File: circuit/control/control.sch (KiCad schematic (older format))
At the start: 24 parts

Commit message: [update] update the circuit diagram
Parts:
- removed 270Ω, 270Ω? (x2): R_US, symbol Device:R_US
- added 270Ω (x4), 270Ω? (x4): R_US, symbol Device:R_US
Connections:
- net GNDPWR: now also 270Ω.2, 270Ω.2, 270Ω.2
- net at RED.1 (K): now also 270Ω.1
- net at GREEN.1 (K): now also 270Ω.1
- net at YELLOW.1 (K): now also 270Ω.1
- net at primary.1 (QB): now also 270Ω?.2; no longer Q?.3 (B)
- net at primary.15 (QA): now also 270Ω?.2; no longer Q?.3 (B)
- net at primary.2 (QC): now also 270Ω?.2; no longer Q?.3 (B)
- net at primary.3 (QD): now also 270Ω?.2; no longer Q?.3 (B)
- net at primary.4 (QE): now also 270Ω.2; no longer Q?.3 (B)
- new net: 270Ω?.1, Q?.3 (B) (x4)
- new net: 270Ω.1, Q?.3 (B)
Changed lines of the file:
@@
 Wire Wire Line
 	8250 3850 8250 5100
-$Comp
-L Device:R_US 270Ω
-U 1 1 6139C615
-P 9750 4650
-F 0 "270Ω" H 9818 4696 50  0000 L CNN
-F 1 "R_US" H 9818 4605 50  0000 L CNN
-F 2 "" V 9790 4640 50  0001 C CNN
-F 3 "~" H 9750 4650 50  0001 C CNN
-	1    9750 4650
-	1    0    0    -1
-$EndComp
 Wire Wire Line
 	9750 4350 9750 4500
-$Comp
-L Device:R_US 270Ω?
-U 1 1 613AA82A
-P 9300 4650
-F 0 "270Ω?" H 9368 4696 50  0000 L CNN
-F 1 "R_US" H 9368 4605 50  0000 L CNN
-F 2 "" V 9340 4640 50  0001 C CNN
-F 3 "~" H 9300 4650 50  0001 C CNN
-	1    9300 4650
-	1    0    0    -1
-$EndComp
 Wire Wire Line
 	9300 4350 9300 4500
@@
 Wire Wire Line
 	9300 4800 9300 5250
-$Comp
-L Device:R_US 270Ω?
-U 1 1 613AB612
-P 8850 4650
-F 0 "270Ω?" H 8918 4696 50  0000 L CNN
-F 1 "R_US" H 8918 4605 50  0000 L CNN
-F 2 "" V 8890 4640 50  0001 C CNN
-F 3 "~" H 8850 4650 50  0001 C CNN
-	1    8850 4650
-	1    0    0    -1
-$EndComp
 Wire Wire Line
 	8850 4350 8850 4500
@@
 	9650 1950 9650 2600
 Wire Wire Line
-	6750 2150 6750 3850
-Wire Wire Line
-	6850 3850 6850 2950
-Wire Wire Line
 	6850 2950 9350 2950
 Wire Wire Line
 	9350 2950 9350 1750
 Wire Wire Line
-	6950 3850 6950 3100
-Wire Wire Line
 	6950 3100 8700 3100
 Wire Wire Line
 	8700 3100 8700 1850
 Wire Wire Line
-	7050 3850 7050 3250
-Wire Wire Line
 	7050 3250 7950 3250
 Wire Wire Line
@@
 Wire Wire Line
 	7250 3400 7150 3400
-Wire Wire Line
-	7150 3400 7150 3850
 Wire Wire Line
 	7250 2050 7250 3400
@@
 Wire Wire Line
 	2650 2550 2650 2900
+$Comp
+L Device:R_US 270Ω?
+U 1 1 61287539
+P 6850 3600
+F 0 "270Ω?" H 6918 3646 50  0001 L CNN
+F 1 "R_US" H 6918 3555 50  0001 L CNN
+F 2 "" V 6890 3590 50  0001 C CNN
+F 3 "~" H 6850 3600 50  0001 C CNN
+	1    6850 3600
+	1    0    0    -1
+$EndComp
+$Comp
+L Device:R_US 270Ω?
+U 1 1 6128753F
+P 6950 3600
+F 0 "270Ω?" H 7018 3646 50  0001 L CNN
+F 1 "R_US" H 7018 3555 50  0001 L CNN
+F 2 "" V 6990 3590 50  0001 C CNN
+F 3 "~" H 6950 3600 50  0001 C CNN
+	1    6950 3600
+	1    0    0    -1
+$EndComp
+$Comp
+L Device:R_US 270Ω?
+U 1 1 61287545
+P 7050 3600
+F 0 "270Ω?" H 7118 3646 50  0001 L CNN
+F 1 "R_US" H 7118 3555 50  0001 L CNN
+F 2 "" V 7090 3590 50  0001 C CNN
+F 3 "~" H 7050 3600 50  0001 C CNN
+	1    7050 3600
+	1    0    0    -1
+$EndComp
+Wire Wire Line
+	6750 3750 6750 3850
+Wire Wire Line
+	6850 3750 6850 3850
+Wire Wire Line
+	6950 3750 6950 3850
+Wire Wire Line
+	7050 3850 7050 3750
+Wire Wire Line
+	7150 3750 7150 3850
+Wire Wire Line
+	7150 3450 7150 3400
+Wire Wire Line
+	6850 2950 6850 3450
+Wire Wire Line
+	6950 3450 6950 3100
+Wire Wire Line
+	7050 3250 7050 3450
+$Comp
+L Device:R_US 270Ω
+U 1 1 6128754B
+P 7150 3600
+F 0 "270Ω" H 7218 3646 50  0000 L CNN
+F 1 "R_US" H 7218 3555 50  0000 L CNN
+F 2 "" V 7190 3590 50  0001 C CNN
+F 3 "~" H 7150 3600 50  0001 C CNN
+	1    7150 3600
+	1    0    0    -1
+$EndComp
+$Comp
+L Device:R_US 270Ω?
+U 1 1 61287533
+P 6750 3600
+F 0 "270Ω?" H 6818 3646 50  0001 L CNN
+F 1 "R_US" H 6818 3555 50  0001 L CNN
+F 2 "" V 6790 3590 50  0001 C CNN
+F 3 "~" H 6750 3600 50  0001 C CNN
+	1    6750 3600
+	1    0    0    -1
+$EndComp
+Wire Wire Line
+	6750 3450 6750 2150
+$Comp
+L Device:R_US 270Ω
+U 1 1 612C32C9
+P 8850 4650
+F 0 "270Ω" H 8918 4696 50  0000 L CNN
+F 1 "R_US" H 8918 4605 50  0000 L CNN
+F 2 "" V 8890 4640 50  0001 C CNN
+F 3 "~" H 8850 4650 50  0001 C CNN
+	1    8850 4650
+	1    0    0    -1
+$EndComp
+$Comp
+L Device:R_US 270Ω
+U 1 1 612C81D5
+P 9300 4650
+F 0 "270Ω" H 9368 4696 50  0000 L CNN
+F 1 "R_US" H 9368 4605 50  0000 L CNN
+F 2 "" V 9340 4640 50  0001 C CNN
+F 3 "~" H 9300 4650 50  0001 C CNN
+	1    9300 4650
+	1    0    0    -1
+$EndComp
+$Comp
+L Device:R_US 270Ω
+U 1 1 612CBD21
+P 9750 4650
+F 0 "270Ω" H 9818 4696 50  0000 L CNN
+F 1 "R_US" H 9818 4605 50  0000 L CNN
+F 2 "" V 9790 4640 50  0001 C CNN
+F 3 "~" H 9750 4650 50  0001 C CNN
+	1    9750 4650
+	1    0    0    -1
+$EndComp
 $EndSCHEMATC

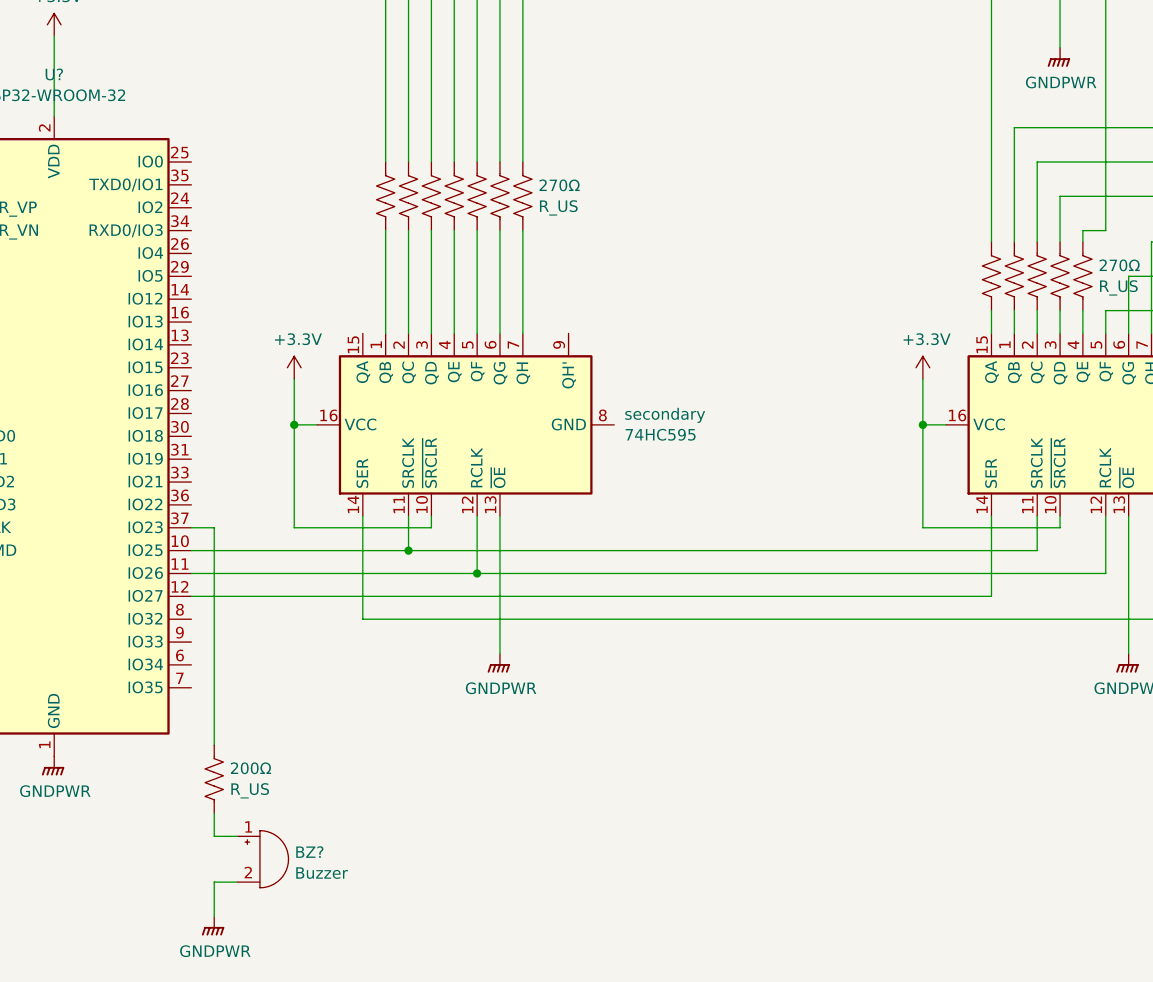
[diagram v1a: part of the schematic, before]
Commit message: [update] update the cicuit diagram
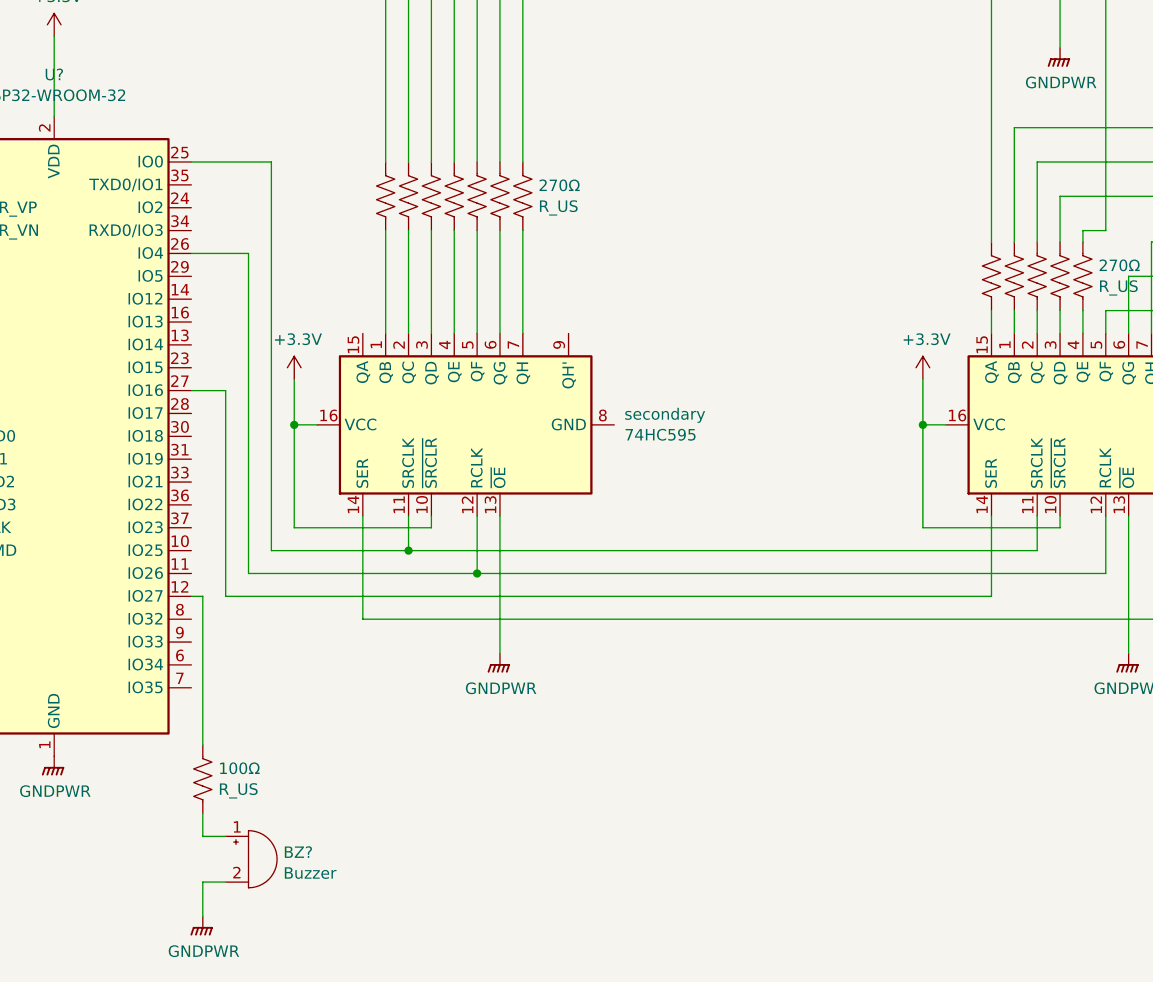
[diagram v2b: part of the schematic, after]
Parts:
- renumbered 200Ω to 100Ω
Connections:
- net at primary.11 (SRCLK), secondary.11 (SRCLK): now also U?.25 (IO0); no longer U?.10 (IO25)
- net at primary.12 (RCLK), secondary.12 (RCLK): now also U?.26 (IO4); no longer U?.11 (IO26)
- net at U?.12 (IO27): now also 100Ω.1; no longer primary.14 (SER)
- net at U?.27 (IO16): now also primary.14 (SER)
- net at U?.37 (IO23): no longer 100Ω.1
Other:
- moved on the sheet: 100Ω, BZ?
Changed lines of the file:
@@
-$EndComp
-$Comp
-L Device:Buzzer BZ?
-U 1 1 6126BBFF
-P 3550 6150
-F 0 "BZ?" H 3702 6179 50  0000 L CNN
-F 1 "Buzzer" H 3702 6088 50  0000 L CNN
-F 2 "" V 3525 6250 50  0001 C CNN
-F 3 "~" V 3525 6250 50  0001 C CNN
-	1    3550 6150
-	1    0    0    -1
 $EndComp
 $Comp
@@
 $EndComp
 Wire Wire Line
-	3250 4700 3350 4700
-Wire Wire Line
-	3350 6050 3450 6050
-Wire Wire Line
-	3450 6250 3350 6250
-Wire Wire Line
-	3350 6250 3350 6400
-$Comp
-L power:GNDPWR #PWR?
-U 1 1 612D5902
-P 3350 6400
-F 0 "#PWR?" H 3350 6200 50  0001 C CNN
-F 1 "GNDPWR" H 3354 6246 50  0000 C CNN
-F 2 "" H 3350 6350 50  0001 C CNN
-F 3 "" H 3350 6350 50  0001 C CNN
-	1    3350 6400
-	1    0    0    -1
-$EndComp
-Wire Wire Line
 	7250 4900 7250 4650
 Wire Wire Line
@@
 	6450 4700 6450 4250
 Connection ~ 6450 4250
-Wire Wire Line
-	3250 5000 6750 5000
 Wire Wire Line
 	6750 5000 6750 4650
@@
 $EndComp
 Wire Wire Line
-	3250 4800 4200 4800
-Wire Wire Line
-	3250 4900 4500 4900
-Connection ~ 4200 4800
-Wire Wire Line
-	4200 4800 6950 4800
-Connection ~ 4500 4900
-Wire Wire Line
-	4500 4900 7250 4900
-Wire Wire Line
 	4000 5100 8250 5100
 Wire Wire Line
@@
 $EndComp
 $Comp
-L Device:R_US 200Ω
-U 1 1 617204BC
-P 3350 5800
-F 0 "200Ω" H 3418 5846 50  0000 L CNN
-F 1 "R_US" H 3418 5755 50  0000 L CNN
-F 2 "" V 3390 5790 50  0001 C CNN
-F 3 "~" H 3350 5800 50  0001 C CNN
-	1    3350 5800
-	1    0    0    -1
-$EndComp
-Wire Wire Line
-	3350 4700 3350 5650
-Wire Wire Line
-	3350 6050 3350 5950
-$Comp
 L power:+3.3V #PWR?
 U 1 1 6174534F
@@
 	1    0    0    -1
 $EndComp
+Wire Wire Line
+	3250 3100 3600 3100
+Wire Wire Line
+	3250 4100 3400 4100
+Wire Wire Line
+	3300 6050 3300 5950
+$Comp
+L Device:R_US 100Ω
+U 1 1 617204BC
+P 3300 5800
+F 0 "100Ω" H 3368 5846 50  0000 L CNN
+F 1 "R_US" H 3368 5755 50  0000 L CNN
+F 2 "" V 3340 5790 50  0001 C CNN
+F 3 "~" H 3300 5800 50  0001 C CNN
+	1    3300 5800
+	1    0    0    -1
+$EndComp
+$Comp
+L power:GNDPWR #PWR?
+U 1 1 612D5902
+P 3300 6400
+F 0 "#PWR?" H 3300 6200 50  0001 C CNN
+F 1 "GNDPWR" H 3304 6246 50  0000 C CNN
+F 2 "" H 3300 6350 50  0001 C CNN
+F 3 "" H 3300 6350 50  0001 C CNN
+	1    3300 6400
+	1    0    0    -1
+$EndComp
+Wire Wire Line
+	3300 6250 3300 6400
+Wire Wire Line
+	3400 6250 3300 6250
+Wire Wire Line
+	3300 6050 3400 6050
+$Comp
+L Device:Buzzer BZ?
+U 1 1 6126BBFF
+P 3500 6150
+F 0 "BZ?" H 3652 6179 50  0000 L CNN
+F 1 "Buzzer" H 3652 6088 50  0000 L CNN
+F 2 "" V 3475 6250 50  0001 C CNN
+F 3 "~" V 3475 6250 50  0001 C CNN
+	1    3500 6150
+	1    0    0    -1
+$EndComp
+Wire Wire Line
+	3250 3500 3500 3500
+Wire Wire Line
+	3600 4800 4200 4800
+Wire Wire Line
+	3600 3100 3600 4800
+Connection ~ 4200 4800
+Wire Wire Line
+	4200 4800 6950 4800
+Wire Wire Line
+	3500 4900 4500 4900
+Wire Wire Line
+	3500 3500 3500 4900
+Connection ~ 4500 4900
+Wire Wire Line
+	4500 4900 7250 4900
+Wire Wire Line
+	3400 5000 6750 5000
+Wire Wire Line
+	3400 4100 3400 5000
+Wire Wire Line
+	3250 5000 3300 5000
+Wire Wire Line
+	3300 5000 3300 5650
 $EndSCHEMATC

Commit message: [update] update circuit diagram
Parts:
- added 10kΩ: R_US, symbol Device:R_US
- added SW?: SW_Push, symbol Switch:SW_Push
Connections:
- net +3V3: now also 10kΩ.2
- net GNDPWR: now also SW?.1
- net at U?.36 (IO22): now also 10kΩ.1, SW?.2
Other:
- moved on the sheet: 100Ω, BZ?, U?
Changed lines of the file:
@@
 L RF_Module:ESP32-WROOM-32 U?
 U 1 1 6124F0F7
-P 2650 4300
-F 0 "U?" H 2650 5881 50  0000 C CNN
-F 1 "ESP32-WROOM-32" H 2650 5790 50  0000 C CNN
-F 2 "RF_Module:ESP32-WROOM-32" H 2650 2800 50  0001 C CNN
-F 3 "https://www.espressif.com/sites/default/files/documentation/esp32-wroom-32_datasheet_en.pdf" H 2350 4350 50  0001 C CNN
-	1    2650 4300
+P 2300 4300
+F 0 "U?" H 2300 5881 50  0000 C CNN
+F 1 "ESP32-WROOM-32" H 2300 5790 50  0000 C CNN
+F 2 "RF_Module:ESP32-WROOM-32" H 2300 2800 50  0001 C CNN
+F 3 "https://www.espressif.com/sites/default/files/documentation/esp32-wroom-32_datasheet_en.pdf" H 2000 4350 50  0001 C CNN
+	1    2300 4300
 	1    0    0    -1
 $EndComp
@@
 L power:GNDPWR #PWR?
 U 1 1 612CC9A8
-P 2650 5700
-F 0 "#PWR?" H 2650 5500 50  0001 C CNN
-F 1 "GNDPWR" H 2654 5546 50  0000 C CNN
-F 2 "" H 2650 5650 50  0001 C CNN
-F 3 "" H 2650 5650 50  0001 C CNN
-	1    2650 5700
+P 2300 5700
+F 0 "#PWR?" H 2300 5500 50  0001 C CNN
+F 1 "GNDPWR" H 2304 5546 50  0000 C CNN
+F 2 "" H 2300 5650 50  0001 C CNN
+F 3 "" H 2300 5650 50  0001 C CNN
+	1    2300 5700
 	1    0    0    -1
 $EndComp
@@
 L power:+3.3V #PWR?
 U 1 1 6174534F
-P 2650 2550
-F 0 "#PWR?" H 2650 2400 50  0001 C CNN
-F 1 "+3.3V" H 2665 2723 50  0000 C CNN
-F 2 "" H 2650 2550 50  0001 C CNN
-F 3 "" H 2650 2550 50  0001 C CNN
-	1    2650 2550
-	1    0    0    -1
-$EndComp
-Wire Wire Line
-	2650 2550 2650 2900
+P 2300 2550
+F 0 "#PWR?" H 2300 2400 50  0001 C CNN
+F 1 "+3.3V" H 2315 2723 50  0000 C CNN
+F 2 "" H 2300 2550 50  0001 C CNN
+F 3 "" H 2300 2550 50  0001 C CNN
+	1    2300 2550
+	1    0    0    -1
+$EndComp
+Wire Wire Line
+	2300 2550 2300 2900
 $Comp
 L Device:R_US 270Ω?
@@
 	1    0    0    -1
 $EndComp
-$Comp
-L Device:R_US 270Ω?
-U 1 1 61287533
-P 6750 3600
-F 0 "270Ω?" H 6818 3646 50  0001 L CNN
-F 1 "R_US" H 6818 3555 50  0001 L CNN
-F 2 "" V 6790 3590 50  0001 C CNN
-F 3 "~" H 6750 3600 50  0001 C CNN
-	1    6750 3600
-	1    0    0    -1
-$EndComp
 Wire Wire Line
 	6750 3450 6750 2150
@@
 $EndComp
 Wire Wire Line
-	3250 3100 3600 3100
-Wire Wire Line
-	3250 4100 3400 4100
-Wire Wire Line
-	3300 6050 3300 5950
+	2950 6050 2950 5950
 $Comp
 L Device:R_US 100Ω
 U 1 1 617204BC
-P 3300 5800
-F 0 "100Ω" H 3368 5846 50  0000 L CNN
-F 1 "R_US" H 3368 5755 50  0000 L CNN
-F 2 "" V 3340 5790 50  0001 C CNN
-F 3 "~" H 3300 5800 50  0001 C CNN
-	1    3300 5800
+P 2950 5800
+F 0 "100Ω" H 3018 5846 50  0000 L CNN
+F 1 "R_US" H 3018 5755 50  0000 L CNN
+F 2 "" V 2990 5790 50  0001 C CNN
+F 3 "~" H 2950 5800 50  0001 C CNN
+	1    2950 5800
 	1    0    0    -1
 $EndComp
@@
 L power:GNDPWR #PWR?
 U 1 1 612D5902
-P 3300 6400
-F 0 "#PWR?" H 3300 6200 50  0001 C CNN
-F 1 "GNDPWR" H 3304 6246 50  0000 C CNN
-F 2 "" H 3300 6350 50  0001 C CNN
-F 3 "" H 3300 6350 50  0001 C CNN
-	1    3300 6400
-	1    0    0    -1
-$EndComp
-Wire Wire Line
-	3300 6250 3300 6400
-Wire Wire Line
-	3400 6250 3300 6250
-Wire Wire Line
-	3300 6050 3400 6050
+P 2950 6400
+F 0 "#PWR?" H 2950 6200 50  0001 C CNN
+F 1 "GNDPWR" H 2954 6246 50  0000 C CNN
+F 2 "" H 2950 6350 50  0001 C CNN
+F 3 "" H 2950 6350 50  0001 C CNN
+	1    2950 6400
+	1    0    0    -1
+$EndComp
+Wire Wire Line
+	2950 6250 2950 6400
+Wire Wire Line
+	3050 6250 2950 6250
+Wire Wire Line
+	2950 6050 3050 6050
 $Comp
 L Device:Buzzer BZ?
 U 1 1 6126BBFF
-P 3500 6150
-F 0 "BZ?" H 3652 6179 50  0000 L CNN
-F 1 "Buzzer" H 3652 6088 50  0000 L CNN
-F 2 "" V 3475 6250 50  0001 C CNN
-F 3 "~" V 3475 6250 50  0001 C CNN
-	1    3500 6150
-	1    0    0    -1
-$EndComp
-Wire Wire Line
-	3250 3500 3500 3500
+P 3150 6150
+F 0 "BZ?" H 3302 6179 50  0000 L CNN
+F 1 "Buzzer" H 3302 6088 50  0000 L CNN
+F 2 "" V 3125 6250 50  0001 C CNN
+F 3 "~" V 3125 6250 50  0001 C CNN
+	1    3150 6150
+	1    0    0    -1
+$EndComp
 Wire Wire Line
 	3600 4800 4200 4800
@@
 	3400 4100 3400 5000
 Wire Wire Line
-	3250 5000 3300 5000
-Wire Wire Line
-	3300 5000 3300 5650
+	2900 5000 2950 5000
+Wire Wire Line
+	2950 5000 2950 5650
+Wire Wire Line
+	2900 3100 3600 3100
+Wire Wire Line
+	2900 3500 3500 3500
+Wire Wire Line
+	2900 4100 3400 4100
+Wire Wire Line
+	2900 4600 3300 4600
+$Comp
+L power:GNDPWR #PWR?
+U 1 1 616229BF
+P 3300 5250
+F 0 "#PWR?" H 3300 5050 50  0001 C CNN
+F 1 "GNDPWR" H 3304 5096 50  0000 C CNN
+F 2 "" H 3300 5200 50  0001 C CNN
+F 3 "" H 3300 5200 50  0001 C CNN
+	1    3300 5250
+	1    0    0    -1
+$EndComp
+$Comp
+L Device:R_US 270Ω?
+U 1 1 61287533
+P 6750 3600
+F 0 "270Ω?" H 6818 3646 50  0001 L CNN
+F 1 "R_US" H 6818 3555 50  0001 L CNN
+F 2 "" V 6790 3590 50  0001 C CNN
+F 3 "~" H 6750 3600 50  0001 C CNN
+	1    6750 3600
+	1    0    0    -1
+$EndComp
+Wire Wire Line
+	3300 4600 3300 4500
+$Comp
+L power:+3.3V #PWR?
+U 1 1 6165DB78
+P 3300 4050
+F 0 "#PWR?" H 3300 3900 50  0001 C CNN
+F 1 "+3.3V" H 3315 4223 50  0000 C CNN
+F 2 "" H 3300 4050 50  0001 C CNN
+F 3 "" H 3300 4050 50  0001 C CNN
+	1    3300 4050
+	1    0    0    -1
+$EndComp
+Wire Wire Line
+	3300 4050 3300 4200
+$Comp
+L Device:R_US 10kΩ
+U 1 1 6165705D
+P 3300 4350
+F 0 "10kΩ" H 3368 4396 50  0000 L CNN
+F 1 "R_US" H 3368 4305 50  0000 L CNN
+F 2 "" V 3340 4340 50  0001 C CNN
+F 3 "~" H 3300 4350 50  0001 C CNN
+	1    3300 4350
+	-1   0    0    1
+$EndComp
+Wire Wire Line
+	3300 4600 3300 4700
+Connection ~ 3300 4600
+Wire Wire Line
+	3300 5100 3300 5250
+$Comp
+L Switch:SW_Push SW?
+U 1 1 616981A3
+P 3300 4900
+F 0 "SW?" H 3300 5185 50  0001 C CNN
+F 1 "SW_Push" H 3300 4852 50  0000 R CNN
+F 2 "" H 3300 5100 50  0001 C CNN
+F 3 "~" H 3300 5100 50  0001 C CNN
+	1    3300 4900
+	0    -1   -1   0
+$EndComp
 $EndSCHEMATC

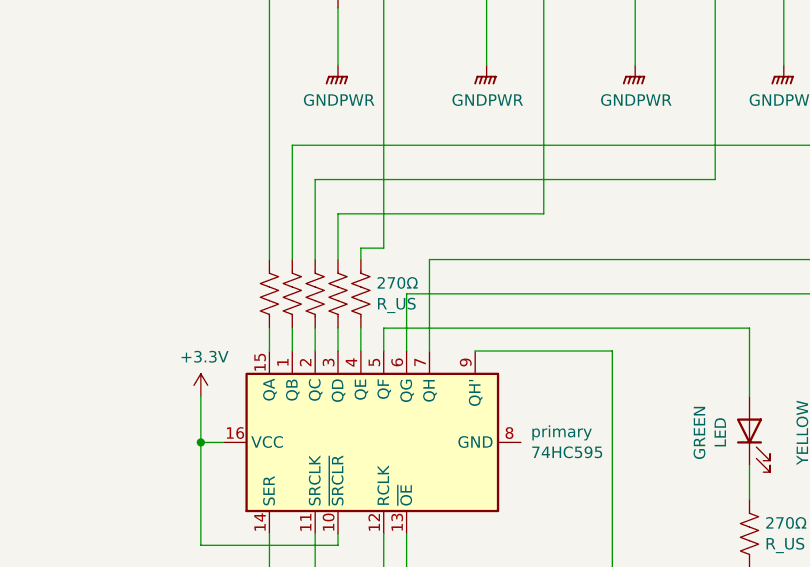
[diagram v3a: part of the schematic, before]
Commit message: [fix] fix the value of resistance in circuit diagram
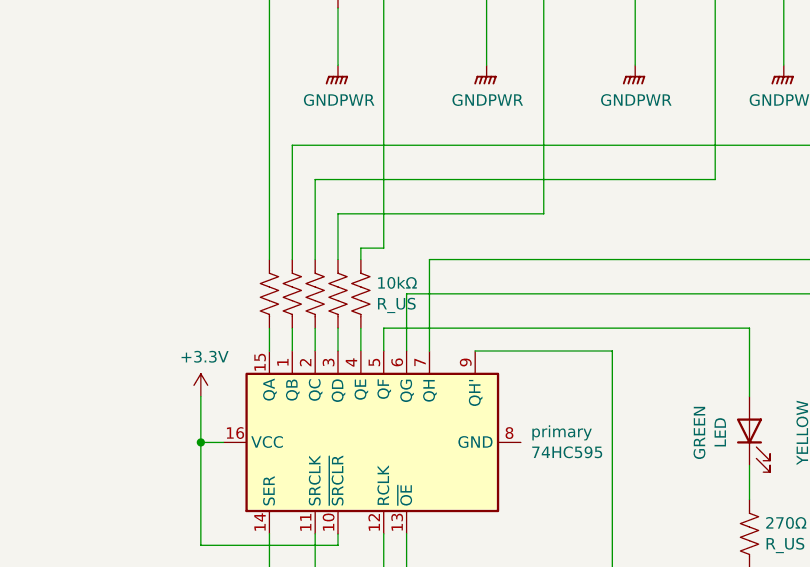
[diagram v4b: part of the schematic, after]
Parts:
- renumbered 270Ω to 10kΩ
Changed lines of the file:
@@
 	7050 3250 7050 3450
 $Comp
-L Device:R_US 270Ω
+L Device:R_US 10kΩ
 U 1 1 6128754B
 P 7150 3600
-F 0 "270Ω" H 7218 3646 50  0000 L CNN
+F 0 "10kΩ" H 7218 3646 50  0000 L CNN
 F 1 "R_US" H 7218 3555 50  0000 L CNN
 F 2 "" V 7190 3590 50  0001 C CNN
